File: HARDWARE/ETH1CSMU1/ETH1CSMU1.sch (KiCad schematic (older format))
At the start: 0 parts

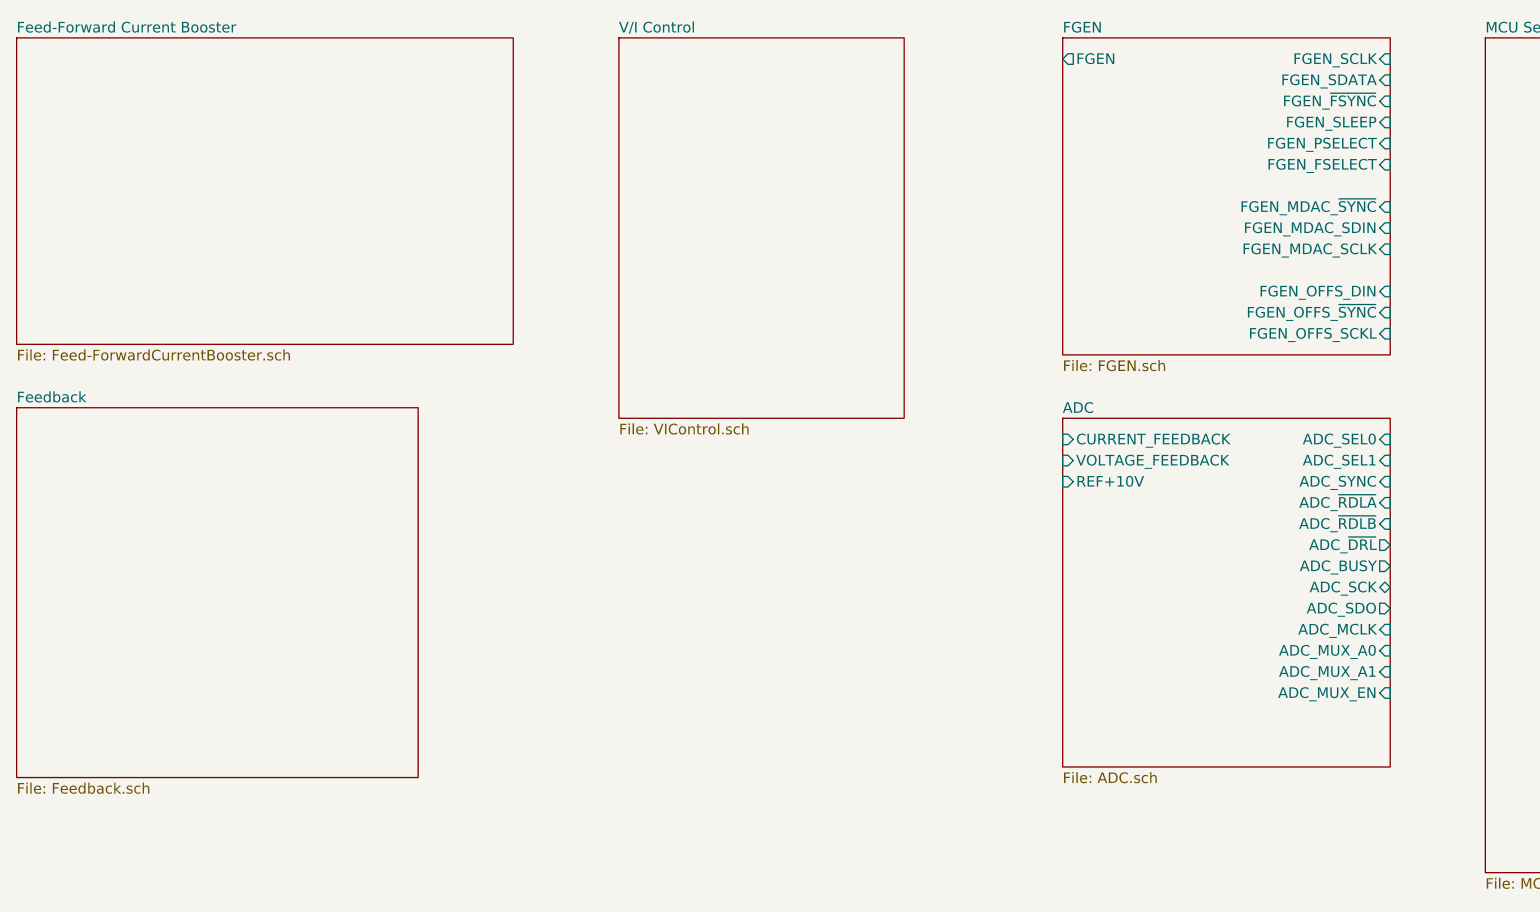
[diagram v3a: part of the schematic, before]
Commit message: Redesigned feedback circuit.
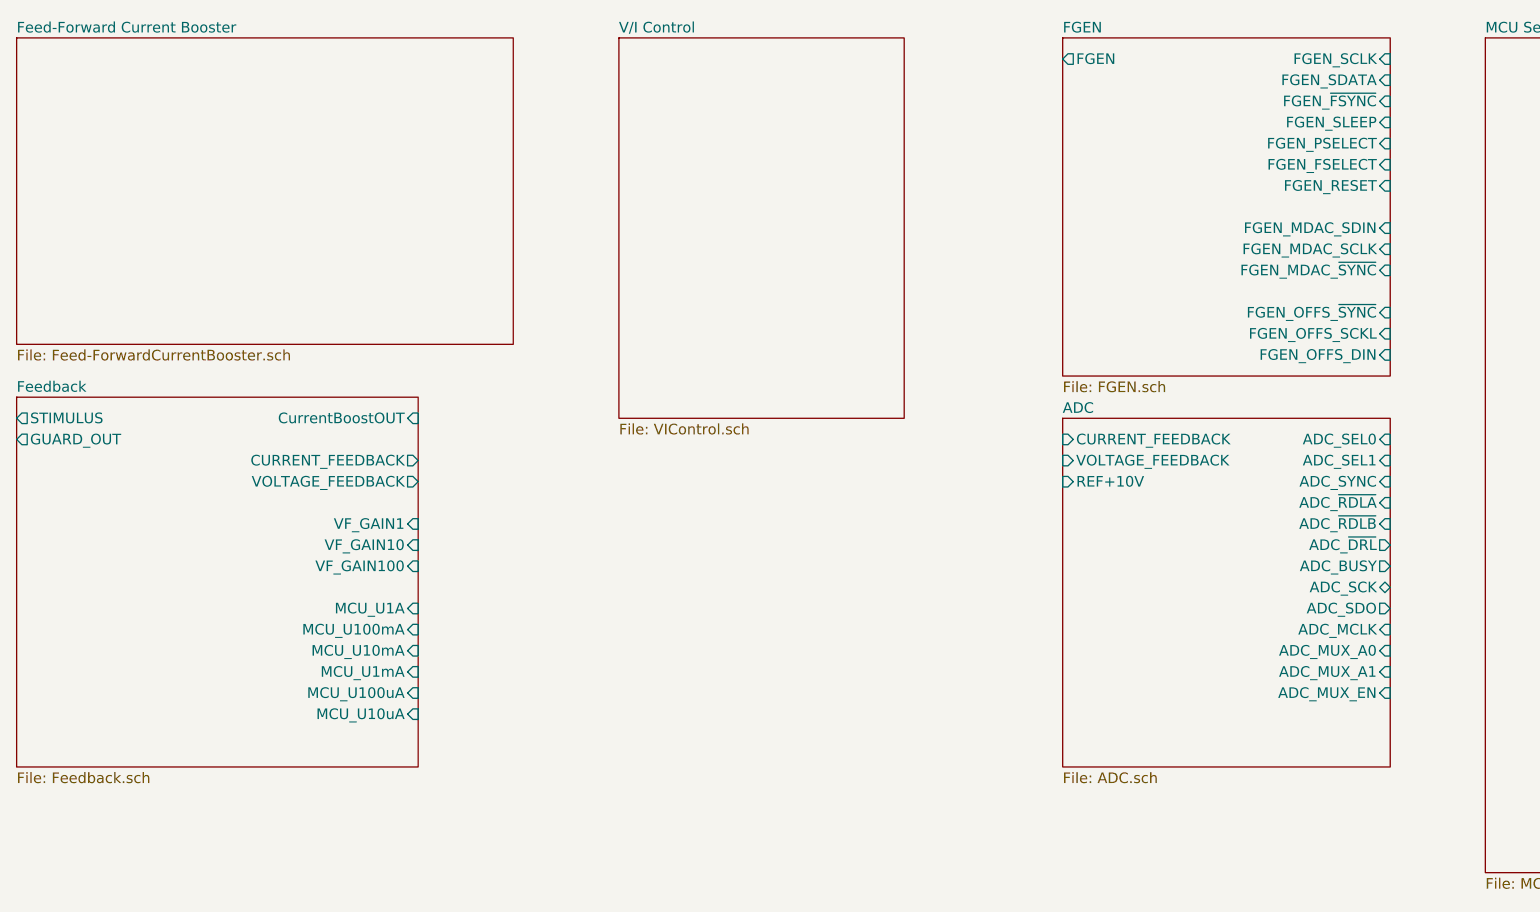
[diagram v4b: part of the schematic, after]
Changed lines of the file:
@@
 $EndSheet
 $Sheet
-S 2600 5100 1900 1750
+S 2600 5050 1900 1750
 U 5BE150E7
 F0 "Feedback" 50
 F1 "Feedback.sch" 50
+F2 "CurrentBoostOUT" I R 4500 5150 50
+F3 "CURRENT_FEEDBACK" O R 4500 5350 50
+F4 "VOLTAGE_FEEDBACK" O R 4500 5450 50
+F5 "STIMULUS" O L 2600 5150 50
+F6 "GUARD_OUT" O L 2600 5250 50
+F7 "VF_GAIN1" I R 4500 5650 50
+F8 "VF_GAIN10" I R 4500 5750 50
+F9 "MCU_U1A" I R 4500 6050 50
+F10 "MCU_U100mA" I R 4500 6150 50
+F11 "MCU_U10mA" I R 4500 6250 50
+F12 "MCU_U1mA" I R 4500 6350 50
+F13 "MCU_U100uA" I R 4500 6450 50
+F14 "VF_GAIN100" I R 4500 5850 50
+F15 "MCU_U10uA" I R 4500 6550 50
 $EndSheet
 $Sheet
@@
 $EndSheet
 $Sheet
-S 7550 3350 1550 1500
+S 7550 3350 1550 1600
 U 5BE3BF24
 F0 "FGEN" 50
@@
 F7 "FGEN_FSELECT" I R 9100 3950 50
 F8 "FGEN" O L 7550 3450 50
-F9 "FGEN_MDAC_~SYNC" I R 9100 4150 50
+F9 "FGEN_MDAC_~SYNC" I R 9100 4450 50
 F10 "FGEN_OFFS_~SYNC" I R 9100 4650 50
 F11 "FGEN_OFFS_SCKL" I R 9100 4750 50
-F12 "FGEN_OFFS_DIN" I R 9100 4550 50
+F12 "FGEN_OFFS_DIN" I R 9100 4850 50
 F13 "FGEN_MDAC_SDIN" I R 9100 4250 50
 F14 "FGEN_MDAC_SCLK" I R 9100 4350 50
+F15 "FGEN_RESET" I R 9100 4050 50
 $EndSheet
 $Sheet

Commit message: Added MUX schematic
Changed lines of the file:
@@
 $Descr A3 16535 11693
 encoding utf-8
-Sheet 1 13
+Sheet 1 14
 Title ""
 Date ""
@@
 F1 "Power.sch" 50
 $EndSheet
+$Sheet
+S 5950 1150 2400 1550
+U 5C477D51
+F0 "MUX" 50
+F1 "MUX.sch" 50
+$EndSheet
 $EndSCHEMATC

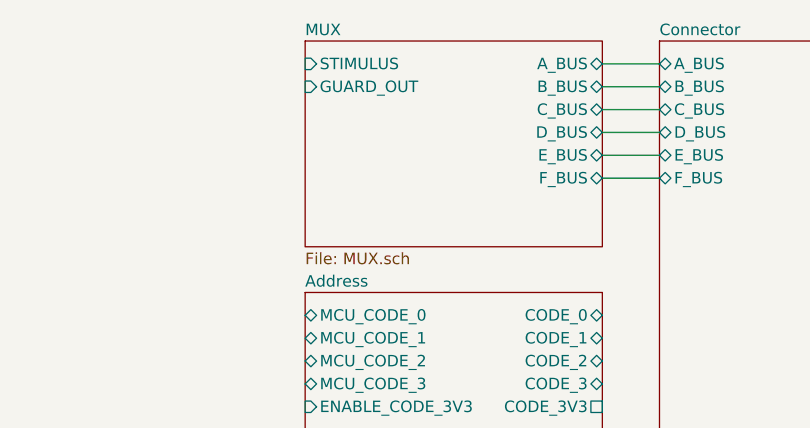
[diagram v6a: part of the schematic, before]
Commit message: Changed BUS mux schematic
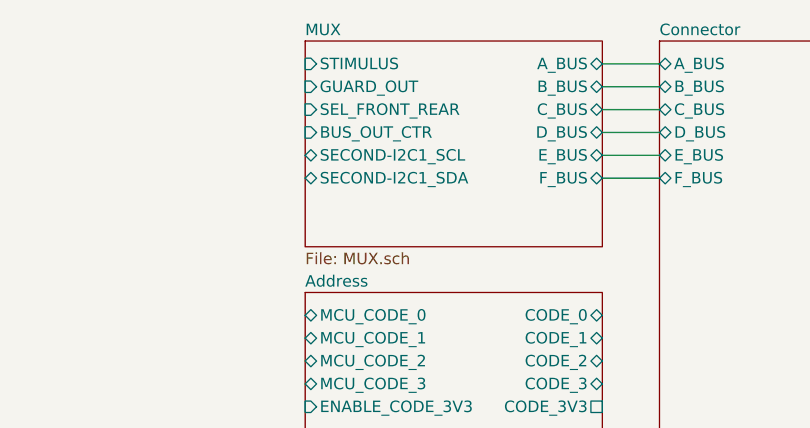
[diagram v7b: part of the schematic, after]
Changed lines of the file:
@@
 F8 "STIMULUS" I L 12950 1250 50
 F9 "GUARD_OUT" I L 12950 1350 50
+F10 "SEL_FRONT_REAR" I L 12950 1450 50
+F11 "SECOND-I2C1_SCL" B L 12950 1650 50
+F12 "SECOND-I2C1_SDA" B L 12950 1750 50
+F13 "BUS_OUT_CTR" I L 12950 1550 50
 $EndSheet
 $Sheet

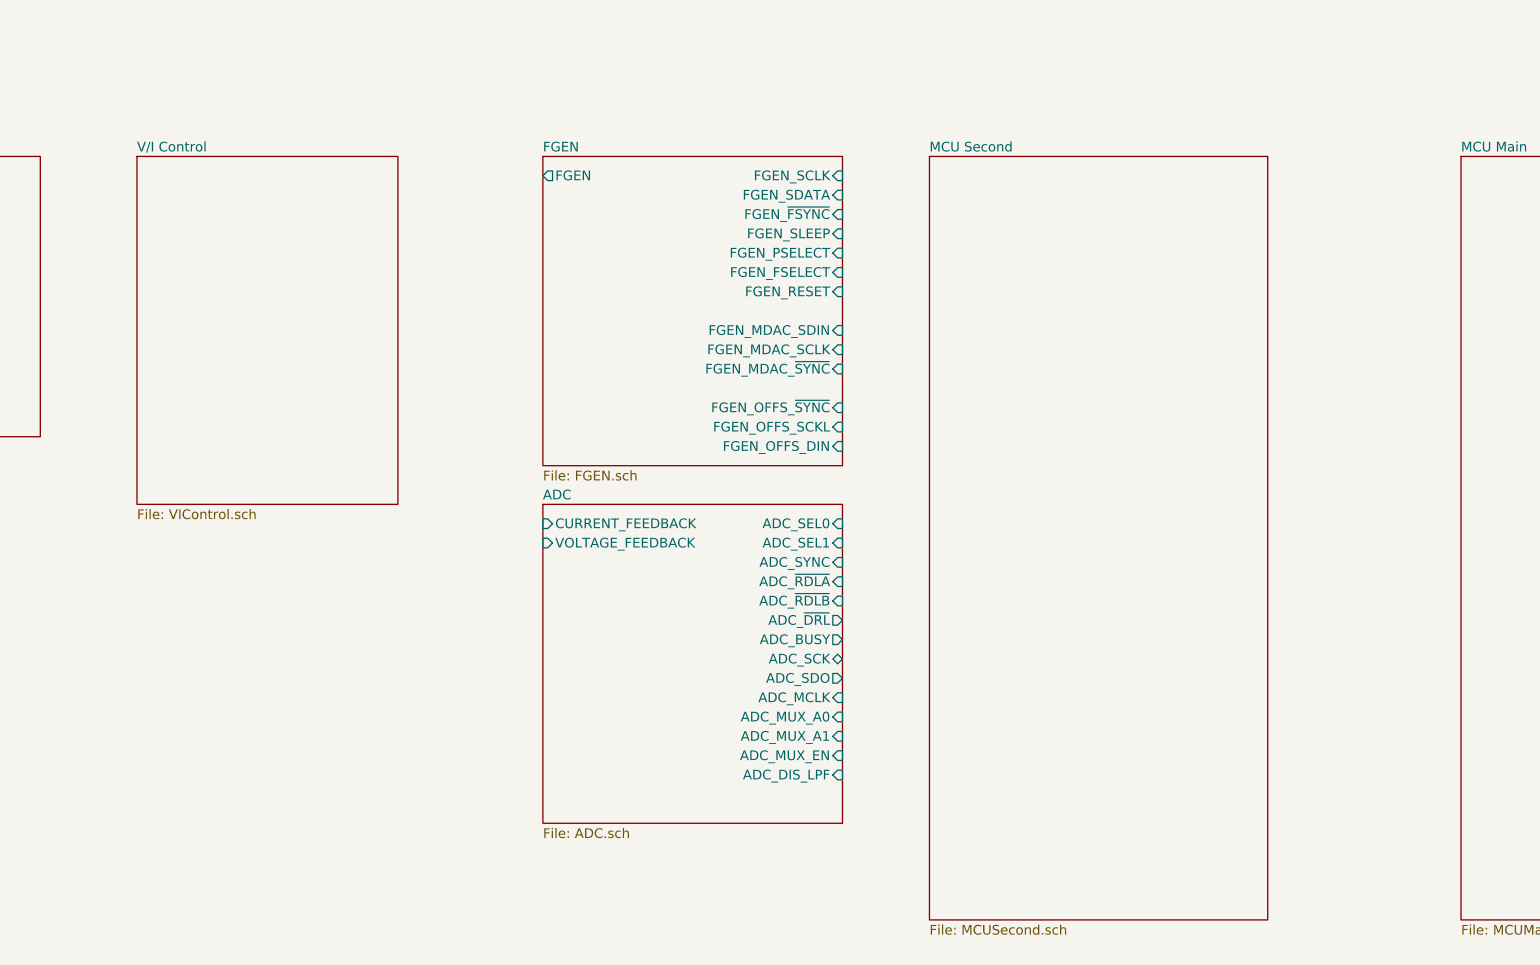
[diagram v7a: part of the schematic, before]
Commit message: Added test circuits, bug fix.
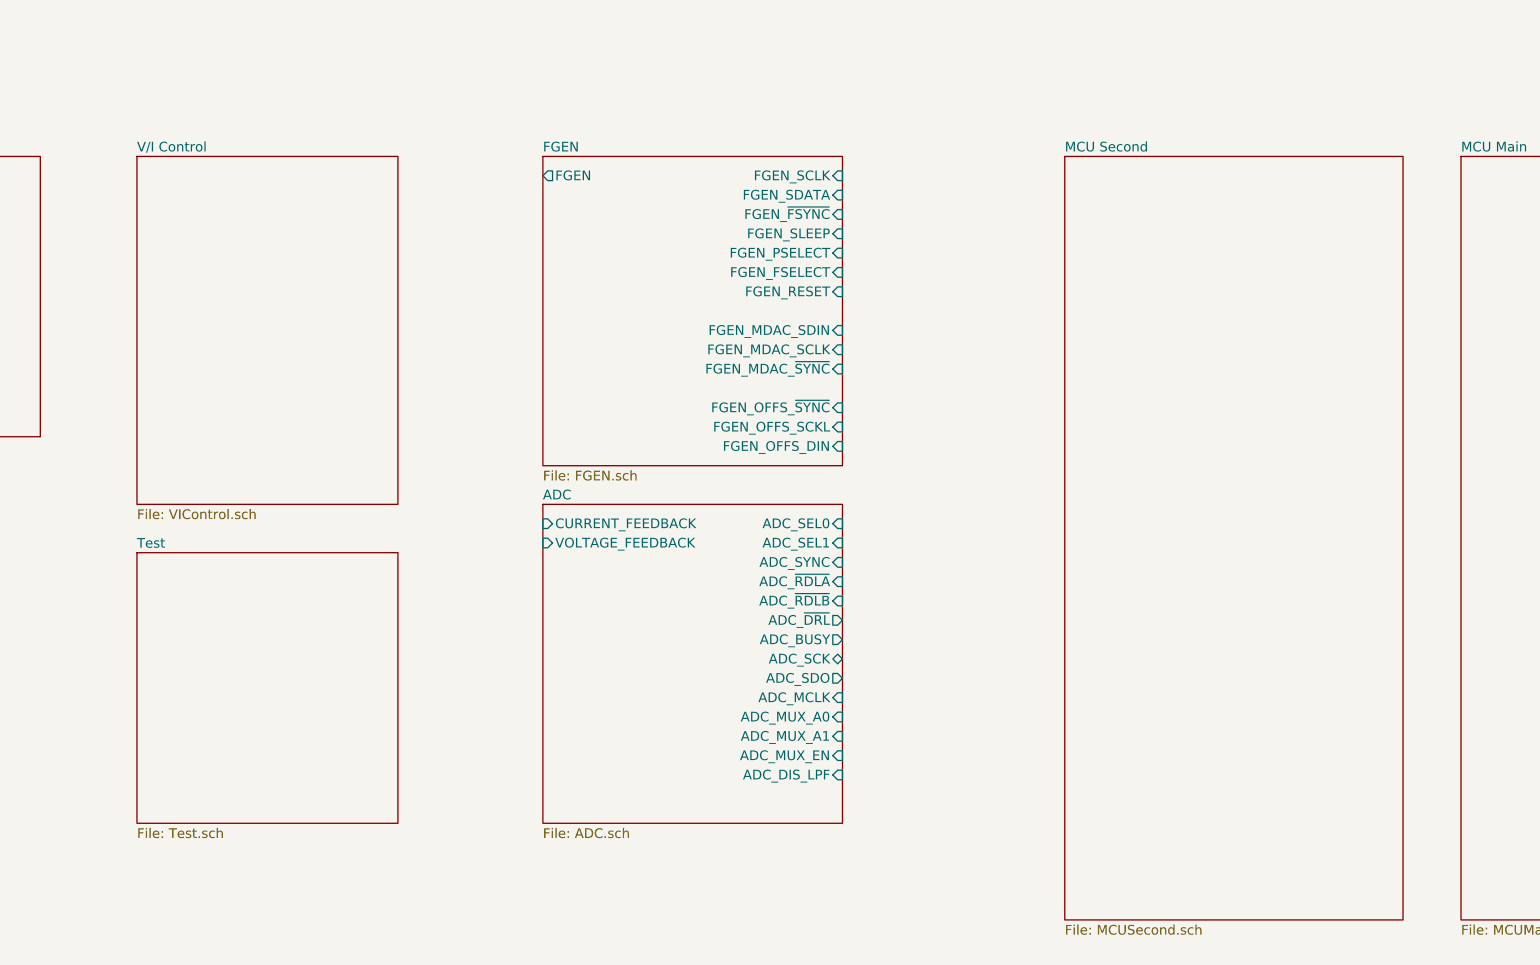
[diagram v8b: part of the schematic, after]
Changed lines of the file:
@@
 $Descr A3 16535 11693
 encoding utf-8
-Sheet 1 15
+Sheet 1 16
 Title ""
 Date ""
@@
 $EndDescr
 $Sheet
-S 8250 3350 1750 3950
+S 8950 3350 1750 3950
 U 5BE0F4FE
 F0 "MCU Second" 50
@@
 Wire Wire Line
 	14500 1750 14250 1750
+$Sheet
+S 4150 5400 1350 1400
+U 5C271DA1
+F0 "Test" 50
+F1 "Test.sch" 50
+$EndSheet
 $EndSCHEMATC
